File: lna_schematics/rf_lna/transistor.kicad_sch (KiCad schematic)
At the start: 24 parts, among them J1 Conn_01x02_Pin, J2 Conn_Coaxial_Small, J3 Conn_Coaxial_Small, U1 L78L05_SOT89, U3 BFP640

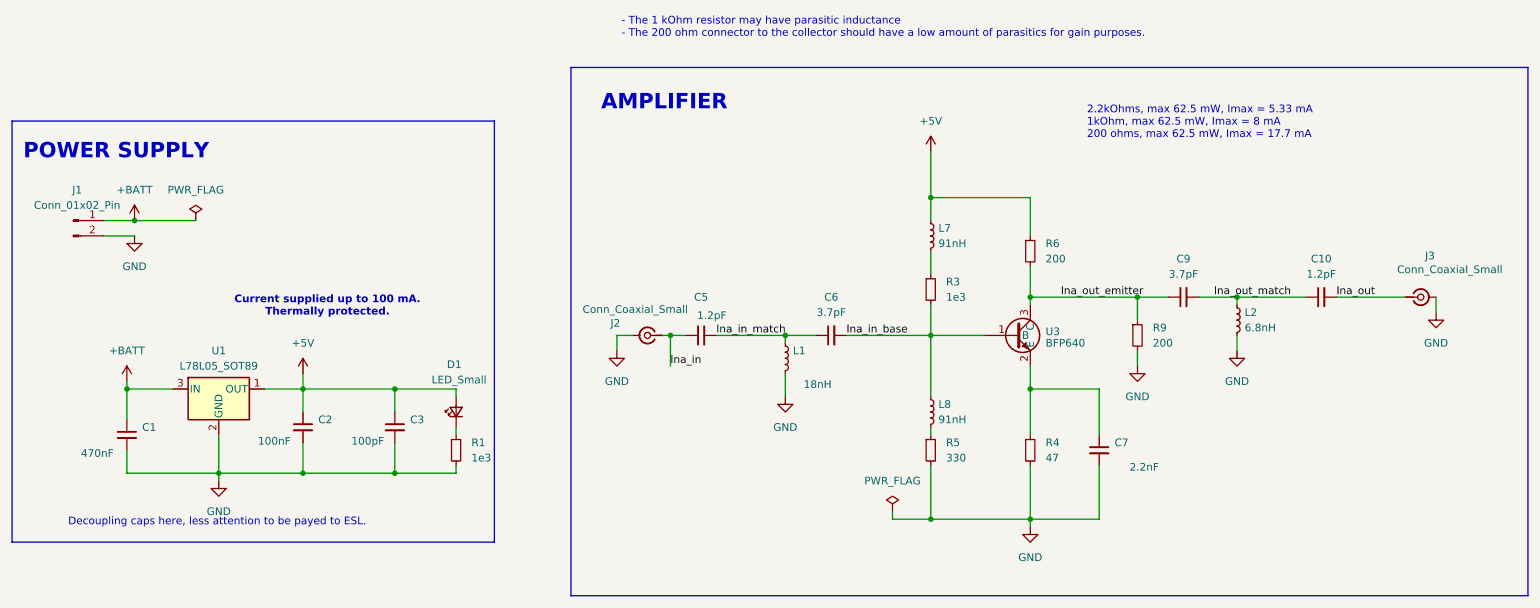
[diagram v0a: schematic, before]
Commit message: [rf_lna] did layout of rf amplifiers for LNA | TODO: create an antenna design for the bottom half
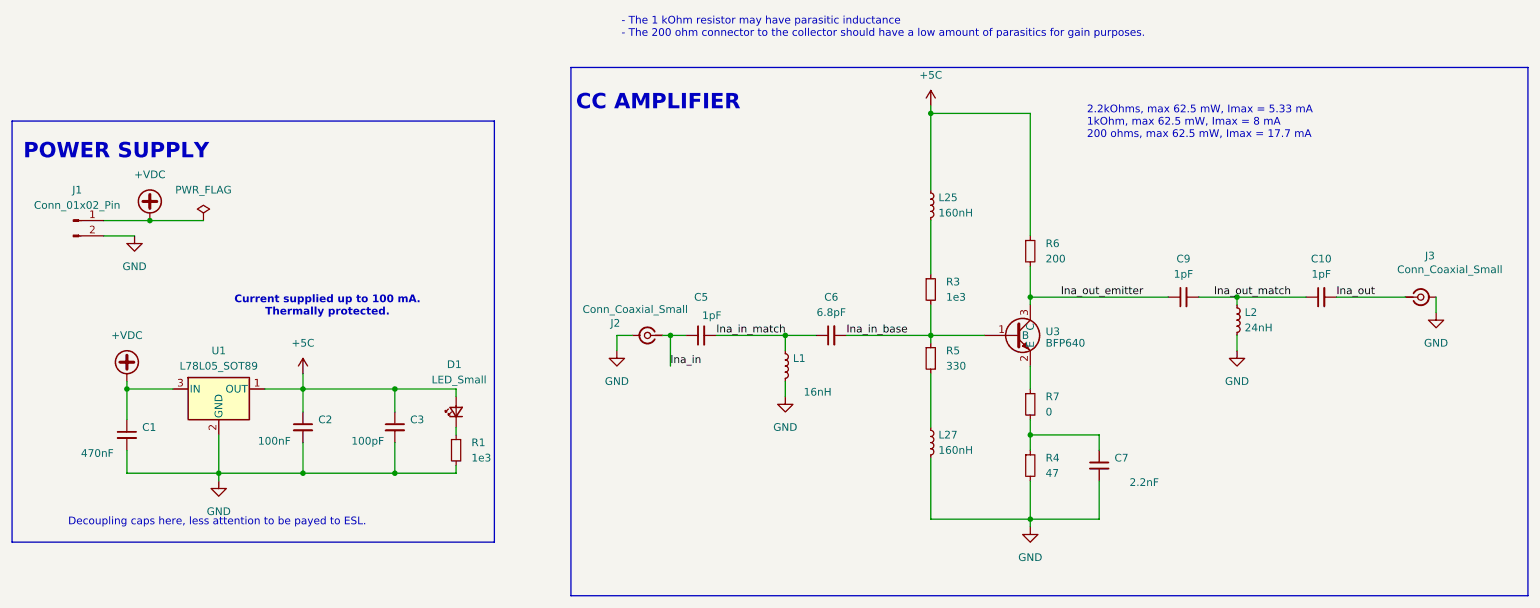
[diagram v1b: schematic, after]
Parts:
- removed L7, L8: 91nH, Inductor_SMD:L_0603_1608Metric, symbol Device:L_Small
- removed R9: 200, Resistor_SMD:R_0402_1005Metric, symbol Device:R_Small
- added L25, L27: 160nH, Inductor_SMD:L_0603_1608Metric, symbol Device:L_Small
- added R7: 0, Capacitor_SMD:C_0402_1005Metric, symbol Device:R_Small
- C10, C5: value 1.2pF -> 1pF; LCSC Part Number C76899 -> C76953; Manufacturing Part Number GJM1555C1H1R2WB01D -> GRM1555C1H1R0CA01D
- C6: value 3.7pF -> 6.8pF; LCSC Part Number C161321 -> C76980; Manufacturing Part Number GJM1555C1H3R6WB01D -> GRM1555C1H6R8CA01D
- C9: value 3.7pF -> 1pF; LCSC Part Number C161321 -> C76953; Manufacturing Part Number GJM1555C1H3R6WB01D -> GRM1555C1H1R0CA01D
- L1: value 18nH -> 16nH; LCSC Part Number C24562 -> C370190; Manufacturing Part Number SDCL1005C18NJTDF -> SDCL1005C16NJTDF
- L2: value 6.8nH -> 24nH; LCSC Part Number C32041 -> C74301; Manufacturing Part Number SDCL1005C6N8JTDF -> SDCL1005C24NJTDF
- R4: footprint Capacitor_SMD:C_0402_1005Metric -> Resistor_SMD:R_0603_1608Metric; LCSC Part Number C4109 -> C23182; Manufacturing Part Number 0402WGF2001TCE -> 0603WAF470JT5E
- R5: LCSC Part Number C11702 -> C25104; Manufacturing Part Number 0402WGF1001TCE -> 0402WGF3300TCE
- R6: LCSC Part Number C25091 -> C25087; Manufacturing Part Number 0402WGF2200TCE -> 0402WGF2000TCE
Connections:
- net GND: now also L27.2; no longer R5.2
- net lna_in_base: now also R5.1
- net at C7.1, R4.1: now also R7.2; no longer U3.2 (E)
- net at R3.1: now also L25.2
- net +5V renamed +5C
- net +5C: now also L25.1
- net +BATT renamed +VDC
- new net: L27.1, R5.2
- new net: R7.1, U3.2 (E)
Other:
- note added: "CC AMPLIFIER"
- note removed: "AMPLIFIER"
- moved on the sheet: C7, L1, R4
